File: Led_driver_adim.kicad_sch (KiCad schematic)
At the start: 12 parts, among them IC8 A6214KLKTR-T

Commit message: finished boarD
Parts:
- C53: LCSC (none) -> C96446
- C54: LCSC (none) -> C19666
- C55: LCSC (none) -> C15849
- C56, C57: LCSC (none) -> C14663
- D7: LCSC (none) -> C8678
- IC8: LCSC (none) -> C146400
- L8: LCSC (none) -> C5127262
- R25: LCSC (none) -> C25804
- R26: LCSC (none) -> C22975
- R27: LCSC (none) -> C23175
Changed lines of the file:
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@@
+			)
+		)
+		(property "LCSC" "C14663"
+			(at 157.48 71.12 0)
+			(effects
+				(font
+					(size 1.27 1.27)
+				)
+				(hide yes)
 			)
 		)
@@
 		)
 		(property "Description" "Unpolarized capacitor, small symbol"
+			(at 93.98 69.85 0)
+			(effects
+				(font
+					(size 1.27 1.27)
+				)
+				(hide yes)
+			)
+		)
+		(property "LCSC" "C96446"
 			(at 93.98 69.85 0)
 			(effects
@@
 			)
 		)
+		(property "LCSC" "C146400"
+			(at 119.38 73.66 0)
+			(effects
+				(font
+					(size 1.27 1.27)
+				)
+				(hide yes)
+			)
+		)
 		(pin "8"
 		)
@@
 		)
 		(property "Description" "1/4W Resistor"
+			(at 81.28 87.63 0)
+			(effects
+				(font
+					(size 1.27 1.27)
+				)
+				(hide yes)
+			)
+		)
+		(property "LCSC" "C22975"
 			(at 81.28 87.63 0)
 			(effects
@@
 			)
 		)
+		(property "LCSC" "C5127262"
+			(at 171.45 67.31 0)
+			(effects
+				(font
+					(size 1.27 1.27)
+				)
+				(hide yes)
+			)
+		)
 		(pin "2"
 		)
@@
 			)
 		)
+		(property "LCSC" "C19666"
+			(at 100.33 69.85 0)
+			(effects
+				(font
+					(size 1.27 1.27)
+				)
+				(hide yes)
+			)
+		)
 		(pin "1"
 		)
@@
 		)
 		(property "Description" "1/4W Resistor"
+			(at 111.76 72.39 0)
+			(effects
+				(font
+					(size 1.27 1.27)
+				)
+				(hide yes)
+			)
+		)
+		(property "LCSC" "C23175"
 			(at 111.76 72.39 0)
 			(effects
@@
 			)
 		)
+		(property "LCSC" ""
+			(at 175.26 78.74 0)
+			(effects
+				(font
+					(size 1.27 1.27)
+				)
+			)
+		)
 		(pin "2"
 		)
@@
 					(size 1.27 1.27)
 				)
+			)
+		)
+		(property "LCSC" "C8678"
+			(at 166.37 71.12 0)
+			(effects
+				(font
+					(size 1.27 1.27)
+				)
+				(hide yes)
 			)
 		)
@@
 			)
 		)
+		(property "LCSC" "C15849"
+			(at 111.76 86.36 0)
+			(effects
+				(font
+					(size 1.27 1.27)
+				)
+				(hide yes)
+			)
+		)
 		(pin "1"
 		)
@@
 			)
 		)
+		(property "LCSC" "C14663"
+			(at 175.26 90.17 0)
+			(effects
+				(font
+					(size 1.27 1.27)
+				)
+				(hide yes)
+			)
+		)
 		(pin "1"
 		)
@@
 			(at 81.28 74.93 0)
 			(effects
+				(font
+					(size 1.27 1.27)
+				)
+				(hide yes)
+			)
+		)
+		(property "LCSC" "C25804"
+			(at 81.28 74.93 0)
+			(effects

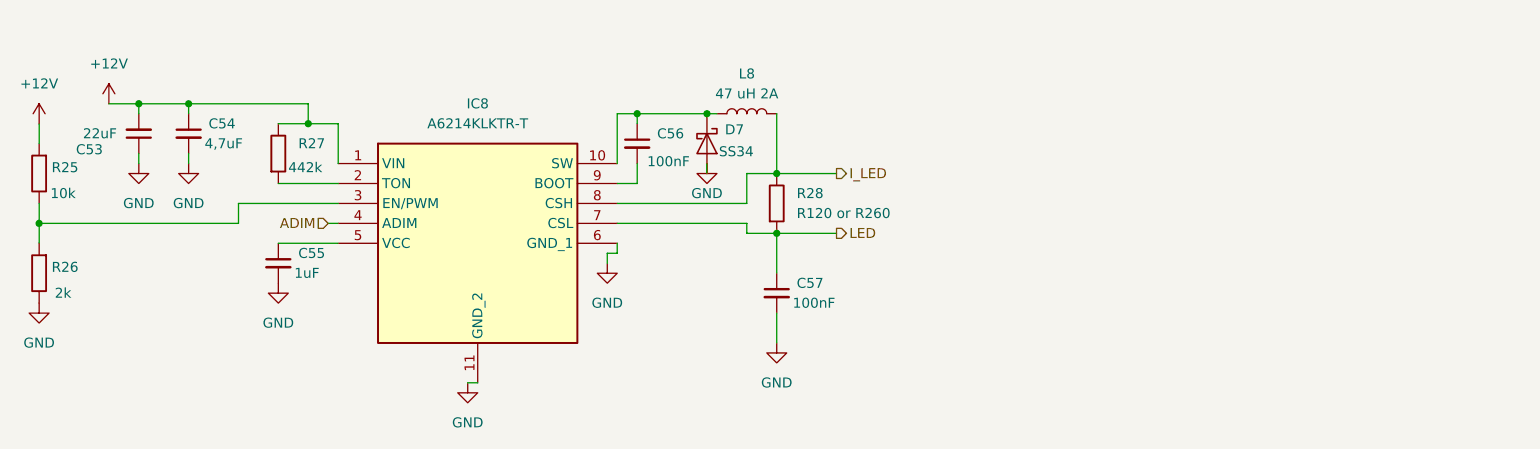
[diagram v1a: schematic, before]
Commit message: Added current sense amplifier, reduced one ADC, changed elec cap to tantals, to review
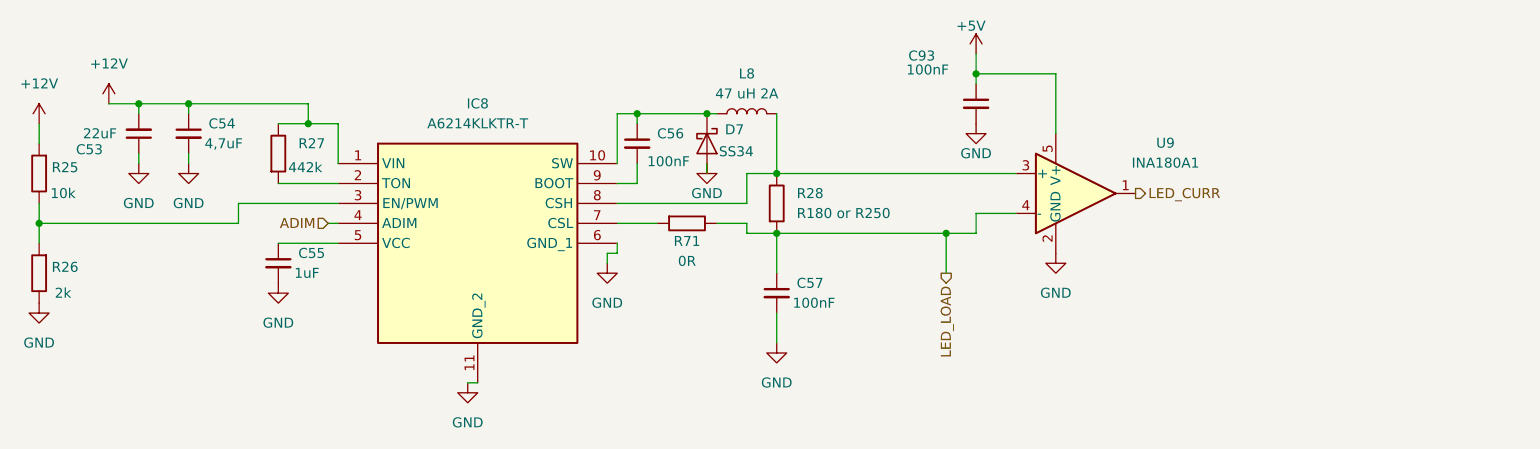
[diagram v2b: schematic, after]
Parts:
- added C93: 100nF, Capacitor_SMD:C_0603_1608Metric_Pad1.08x0.95mm_HandSolder, symbol Device:C_Small
- added R71: 0R, Capacitor_SMD:C_0402_1005Metric_Pad0.74x0.62mm_HandSolder, symbol PCM_SL_Resistors:Resistor
- added U9: INA180A1, Package_TO_SOT_SMD:SOT-23-5, symbol Amplifier_Current:INA180A1
- R28: value R120 or R260 -> R180 or R250
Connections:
- net GND: now also C93.2, U9.2 (GND)
- net I_LED: no longer names the net of IC8.8 (CSH), L8.2, R28.2
- net I_LED: now also U9.3 (+)
- net LED renamed LED_LOAD
- net LED_LOAD: now also R71.2, U9.4 (-); no longer IC8.7 (CSL)
- new net: IC8.7 (CSL), R71.1
- new net +5V: C93.1, U9.5 (V+)
- new net LED_CURR: U9.1

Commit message: Added low pass filters at current sense amp outputs and pull ups on cs pins, DRC done
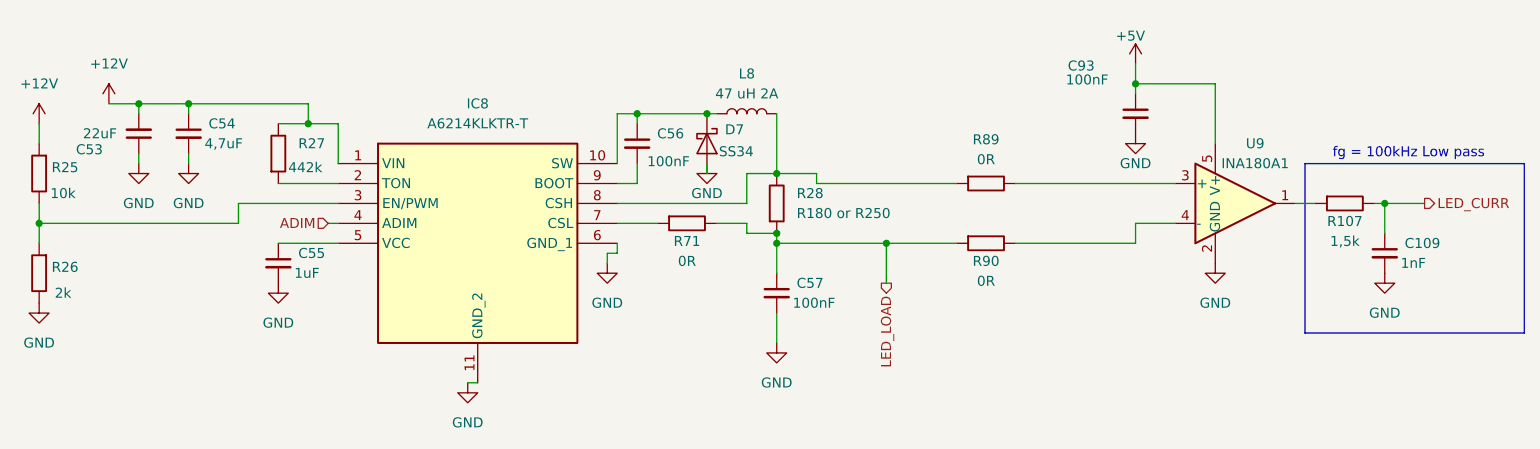
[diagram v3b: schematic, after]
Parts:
- added C109: 1nF, Capacitor_SMD:C_0402_1005Metric_Pad0.74x0.62mm_HandSolder, symbol Device:C_Small
- added R107: 1,5k, Resistor_SMD:R_0402_1005Metric_Pad0.72x0.64mm_HandSolder, symbol PCM_SL_Resistors:Resistor
- added R89, R90: 0R, Resistor_SMD:R_0402_1005Metric_Pad0.72x0.64mm_HandSolder, symbol PCM_SL_Resistors:Resistor
- R71: footprint Capacitor_SMD:C_0402_1005Metric_Pad0.74x0.62mm_HandSolder -> Resistor_SMD:R_0402_1005Metric_Pad0.72x0.64mm_HandSolder
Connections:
- net GND: now also C109.2
- net LED_CURR: now also C109.1, R107.2; no longer U9.1
- net LED_LOAD: now also R90.1; no longer U9.4 (-)
- net at IC8.8 (CSH), L8.2, R28.2: now also R89.1; no longer U9.3 (+)
- new net: R89.2, U9.3 (+)
- new net: R107.1, U9.1
- new net: R90.2, U9.4 (-)
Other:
- note added: "fg = 100kHz Low pass"
- moved on the sheet: C93, U9
